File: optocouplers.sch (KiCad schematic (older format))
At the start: 20 parts, among them J901 Conn_01x04, Q901 MMBT5551L, U901 EL3H7(C)(TA)-G, U902 EL3H7(C)(TA)-G

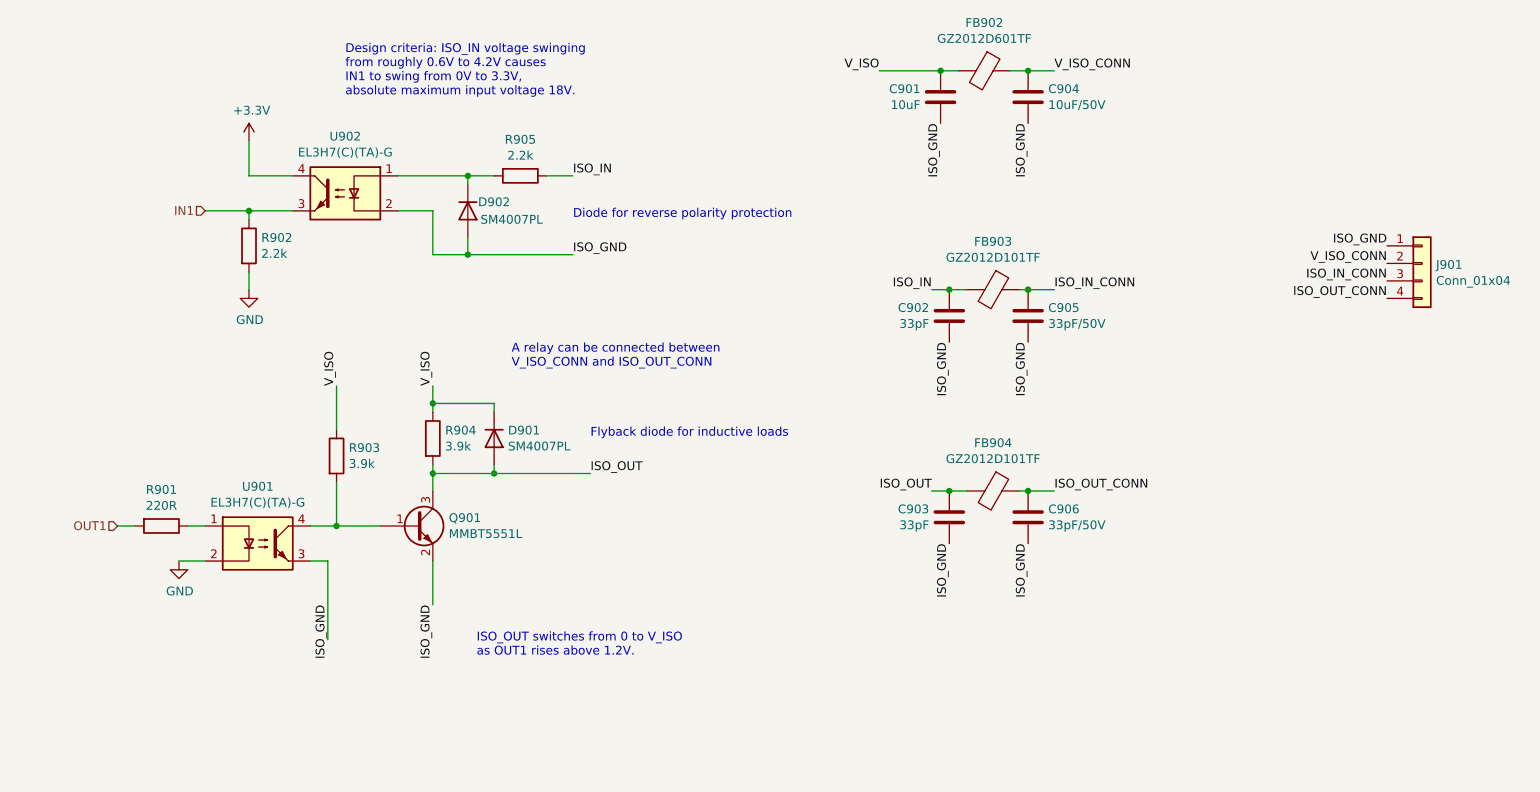
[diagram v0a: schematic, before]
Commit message: Add an unpopulated pad for extra opto output pullup
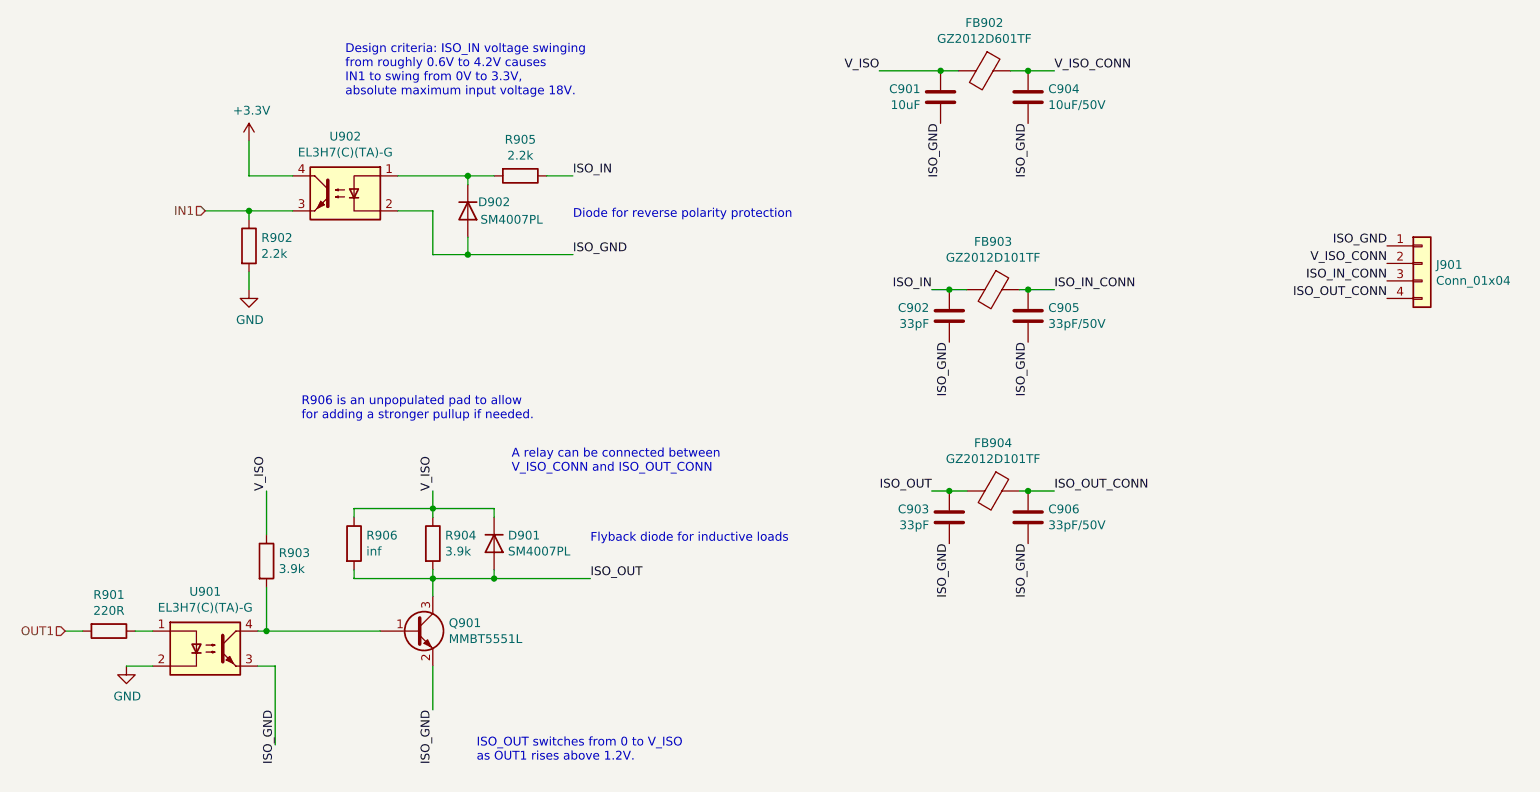
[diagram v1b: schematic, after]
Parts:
- added R906: inf, Resistor_SMD:R_0805_2012Metric, symbol Device:R
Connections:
- net ISO_OUT: now also R906.2
- net V_ISO: now also R906.1
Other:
- note added: "R906 is an unpopulated pad to allow\nfor adding a stronger pullup if needed."
- moved on the sheet: D901, Q901, R901, R903, R904, U901
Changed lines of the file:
@@
 $Descr A4 11693 8268
 encoding utf-8
-Sheet 10 11
+Sheet 9 11
 Title "Sailor Hat for ESP32"
 Date ""
@@
 L Device:R R901
 U 1 1 5FB305CD
-P 2350 4300
-F 0 "R901" V 2143 4300 50  0000 C CNN
-F 1 "220R" V 2234 4300 50  0000 C CNN
-F 2 "Resistor_SMD:R_0603_1608Metric" V 2280 4300 50  0001 C CNN
-F 3 "~" H 2350 4300 50  0001 C CNN
-F 4 "C22962" H 2350 4300 50  0001 C CNN "LCSC"
-	1    2350 4300
+P 2050 4900
+F 0 "R901" V 1843 4900 50  0000 C CNN
+F 1 "220R" V 1934 4900 50  0000 C CNN
+F 2 "Resistor_SMD:R_0603_1608Metric" V 1980 4900 50  0001 C CNN
+F 3 "~" H 2050 4900 50  0001 C CNN
+F 4 "C22962" H 2050 4900 50  0001 C CNN "LCSC"
+	1    2050 4900
 	0    1    1    0
 $EndComp
@@
 L power:GND #PWR0901
 U 1 1 5FB3123D
-P 2450 4500
-F 0 "#PWR0901" H 2450 4250 50  0001 C CNN
-F 1 "GND" H 2455 4327 50  0000 C CNN
-F 2 "" H 2450 4500 50  0001 C CNN
-F 3 "" H 2450 4500 50  0001 C CNN
-	1    2450 4500
-	1    0    0    -1
-$EndComp
-Wire Wire Line
-	2450 4500 2600 4500
-Wire Wire Line
-	2600 4300 2500 4300
-Wire Wire Line
-	2200 4300 2100 4300
+P 2150 5100
+F 0 "#PWR0901" H 2150 4850 50  0001 C CNN
+F 1 "GND" H 2155 4927 50  0000 C CNN
+F 2 "" H 2150 5100 50  0001 C CNN
+F 3 "" H 2150 5100 50  0001 C CNN
+	1    2150 5100
+	1    0    0    -1
+$EndComp
+Wire Wire Line
+	2150 5100 2300 5100
+Wire Wire Line
+	2300 4900 2200 4900
+Wire Wire Line
+	1900 4900 1800 4900
 $Comp
 L Transistor_BJT:MMBT5551L Q901
 U 1 1 5FB347F2
-P 3800 4300
-F 0 "Q901" H 3991 4346 50  0000 L CNN
-F 1 "MMBT5551L" H 3991 4255 50  0000 L CNN
-F 2 "Package_TO_SOT_SMD:SOT-23" H 4000 4225 50  0001 L CIN
-F 3 "www.onsemi.com/pub/Collateral/MMBT5550LT1-D.PDF" H 3800 4300 50  0001 L CNN
-F 4 "C41095" H 3800 4300 50  0001 C CNN "LCSC"
-	1    3800 4300
+P 3800 4900
+F 0 "Q901" H 3991 4946 50  0000 L CNN
+F 1 "MMBT5551L" H 3991 4855 50  0000 L CNN
+F 2 "Package_TO_SOT_SMD:SOT-23" H 4000 4825 50  0001 L CIN
+F 3 "www.onsemi.com/pub/Collateral/MMBT5550LT1-D.PDF" H 3800 4900 50  0001 L CNN
+F 4 "C41095" H 3800 4900 50  0001 C CNN "LCSC"
+	1    3800 4900
 	1    0    0    -1
 $EndComp
@@
 L Device:R R903
 U 1 1 5FB354D0
-P 3350 3900
-F 0 "R903" H 3420 3946 50  0000 L CNN
-F 1 "3.9k" H 3420 3855 50  0000 L CNN
-F 2 "Resistor_SMD:R_0603_1608Metric" V 3280 3900 50  0001 C CNN
-F 3 "~" H 3350 3900 50  0001 C CNN
-F 4 "C23018" H 3350 3900 50  0001 C CNN "LCSC"
-	1    3350 3900
+P 2950 4500
+F 0 "R903" H 3020 4546 50  0000 L CNN
+F 1 "3.9k" H 3020 4455 50  0000 L CNN
+F 2 "Resistor_SMD:R_0603_1608Metric" V 2880 4500 50  0001 C CNN
+F 3 "~" H 2950 4500 50  0001 C CNN
+F 4 "C23018" H 2950 4500 50  0001 C CNN "LCSC"
+	1    2950 4500
 	1    0    0    -1
 $EndComp
@@
 L Device:R R904
 U 1 1 5FB36FDC
-P 3900 3800
-F 0 "R904" H 3970 3846 50  0000 L CNN
-F 1 "3.9k" H 3970 3755 50  0000 L CNN
-F 2 "Resistor_SMD:R_0603_1608Metric" V 3830 3800 50  0001 C CNN
-F 3 "~" H 3900 3800 50  0001 C CNN
-F 4 "C23018" H 3900 3800 50  0001 C CNN "LCSC"
-	1    3900 3800
-	1    0    0    -1
-$EndComp
-Wire Wire Line
-	3350 3750 3350 3500
-Wire Wire Line
-	3900 3650 3900 3600
-Wire Wire Line
-	3200 4300 3350 4300
-Wire Wire Line
-	3350 4050 3350 4300
-Connection ~ 3350 4300
-Wire Wire Line
-	3350 4300 3600 4300
-Wire Wire Line
-	3900 3950 3900 4000
-Connection ~ 3900 4000
-Wire Wire Line
-	3900 4000 3900 4100
-Wire Wire Line
-	3900 4500 3900 4750
-Wire Wire Line
-	3300 4950 3300 4500
-Wire Wire Line
-	3300 4500 3200 4500
-Text Label 3900 4750 3    50   ~ 0
-ISO_GND
-Text Label 4800 4000 0    50   ~ 0
+P 3900 4400
+F 0 "R904" H 3970 4446 50  0000 L CNN
+F 1 "3.9k" H 3970 4355 50  0000 L CNN
+F 2 "Resistor_SMD:R_0603_1608Metric" V 3830 4400 50  0001 C CNN
+F 3 "~" H 3900 4400 50  0001 C CNN
+F 4 "C23018" H 3900 4400 50  0001 C CNN "LCSC"
+	1    3900 4400
+	1    0    0    -1
+$EndComp
+Wire Wire Line
+	2950 4350 2950 4100
+Wire Wire Line
+	3900 4250 3900 4200
+Wire Wire Line
+	2900 4900 2950 4900
+Wire Wire Line
+	2950 4650 2950 4900
+Wire Wire Line
+	3900 4550 3900 4600
+Connection ~ 3900 4600
+Wire Wire Line
+	3900 4600 3900 4700
+Wire Wire Line
+	3900 5100 3900 5350
+Wire Wire Line
+	3000 5550 3000 5100
+Wire Wire Line
+	3000 5100 2900 5100
+Text Label 3900 5350 3    50   ~ 0
+ISO_GND
+Text Label 4800 4600 0    50   ~ 0
 ISO_OUT
-Text Label 3350 3500 1    50   ~ 0
+Text Label 2950 4100 1    50   ~ 0
 V_ISO
-Text Label 3900 3500 1    50   ~ 0
+Text Label 3900 4100 1    50   ~ 0
 V_ISO
 Text Label 4700 2750 0    50   ~ 0
@@
 ISO_GND
 Wire Wire Line
-	3900 4000 4250 4000
+	3900 4600 4250 4600
 Text HLabel 2600 2500 0    50   Input ~ 0
 IN1
-Text HLabel 2100 4300 0    50   Input ~ 0
+Text HLabel 1800 4900 0    50   Input ~ 0
 OUT1
 $Comp
 L Device:D D?
 U 1 1 5FC24243
-P 4250 3800
+P 4250 4400
 AR Path="/5C3476D8/5FC24243" Ref="D?"  Part="1"
 AR Path="/5CA65CC5/5FC24243" Ref="D?"  Part="1"
 AR Path="/5F6FAF6E/5FC24243" Ref="D?"  Part="1"
 AR Path="/5FB2AE13/5FC24243" Ref="D901"  Part="1"
-F 0 "D901" V 4204 3879 50  0000 L CNN
-F 1 "SM4007PL" V 4295 3879 50  0000 L CNN
-F 2 "Diode_SMD:D_SOD-123F" H 4250 3800 50  0001 C CNN
-F 3 "~" H 4250 3800 50  0001 C CNN
-F 4 "" V 4250 3800 50  0001 C CNN "Notes"
-F 5 "C64898" H 4250 3800 50  0001 C CNN "LCSC"
-	1    4250 3800
-	0    1    1    0
-$EndComp
-Text Notes 4350 3400 0    50   ~ 0
+F 0 "D901" V 4204 4479 50  0000 L CNN
+F 1 "SM4007PL" V 4295 4479 50  0000 L CNN
+F 2 "Diode_SMD:D_SOD-123F" H 4250 4400 50  0001 C CNN
+F 3 "~" H 4250 4400 50  0001 C CNN
+F 4 "" V 4250 4400 50  0001 C CNN "Notes"
+F 5 "C64898" H 4250 4400 50  0001 C CNN "LCSC"
+	1    4250 4400
+	0    1    1    0
+$EndComp
+Text Notes 4350 4000 0    50   ~ 0
 A relay can be connected between\nV_ISO_CONN and ISO_OUT_CONN
 Wire Wire Line
-	4250 4000 4250 3950
-Connection ~ 4250 4000
-Wire Wire Line
-	4250 4000 4800 4000
-Wire Wire Line
-	4250 3650 4250 3600
-Wire Wire Line
-	4250 3600 3900 3600
-Connection ~ 3900 3600
-Wire Wire Line
-	3900 3600 3900 3500
+	4250 4600 4250 4550
+Connection ~ 4250 4600
+Wire Wire Line
+	4250 4600 4800 4600
+Wire Wire Line
+	4250 4250 4250 4200
+Wire Wire Line
+	4250 4200 3900 4200
+Connection ~ 3900 4200
+Wire Wire Line
+	3900 4200 3900 4100
 $Comp
 L Connector_Generic:Conn_01x04 J901
@@
 Text Notes 3400 1850 0    50   ~ 0
 Design criteria: ISO_IN voltage swinging \nfrom roughly 0.6V to 4.2V causes \nIN1 to swing from 0V to 3.3V,\nabsolute maximum input voltage 18V.
-Text Notes 4150 5050 0    50   ~ 0
+Text Notes 4150 5650 0    50   ~ 0
 ISO_OUT switches from 0 to V_ISO\nas OUT1 rises above 1.2V.
-Text Label 3300 4750 3    50   ~ 0
+Text Label 3000 5350 3    50   ~ 0
 ISO_GND
 Wire Wire Line
@@
 Text Notes 4700 2550 0    50   ~ 0
 Diode for reverse polarity protection
-Text Notes 4800 3800 0    50   ~ 0
+Text Notes 4800 4400 0    50   ~ 0
 Flyback diode for inductive loads
 $Comp
@@
 L SH-ESP32:EL3H7 U901
 U 1 1 5FCB38F6
-P 2900 4400
-F 0 "U901" H 2900 4725 50  0000 C CNN
-F 1 "EL3H7(C)(TA)-G" H 2900 4634 50  0000 C CNN
-F 2 "Package_SO:SOP-4_4.4x2.6mm_P1.27mm" H 2700 4200 50  0001 L CIN
-F 3 "http://www.sharpsme.com/download/pc3h4-epdf" H 2925 4400 50  0001 L CNN
-F 4 "C92243" H 2900 4400 50  0001 C CNN "LCSC"
-	1    2900 4400
-	1    0    0    -1
-$EndComp
+P 2600 5000
+F 0 "U901" H 2600 5325 50  0000 C CNN
+F 1 "EL3H7(C)(TA)-G" H 2600 5234 50  0000 C CNN
+F 2 "Package_SO:SOP-4_4.4x2.6mm_P1.27mm" H 2400 4800 50  0001 L CIN
+F 3 "http://www.sharpsme.com/download/pc3h4-epdf" H 2625 5000 50  0001 L CNN
+F 4 "C92243" H 2600 5000 50  0001 C CNN "LCSC"
+	1    2600 5000
+	1    0    0    -1
+$EndComp
+Connection ~ 2950 4900
+Wire Wire Line
+	2950 4900 3600 4900
+$Comp
+L Device:R R906
+U 1 1 5FC03D50
+P 3450 4400
+F 0 "R906" H 3520 4446 50  0000 L CNN
+F 1 "inf" H 3520 4355 50  0000 L CNN
+F 2 "Resistor_SMD:R_0805_2012Metric" V 3380 4400 50  0001 C CNN
+F 3 "~" H 3450 4400 50  0001 C CNN
+F 4 "" H 3450 4400 50  0001 C CNN "LCSC"
+	1    3450 4400
+	1    0    0    -1
+$EndComp
+Wire Wire Line
+	3450 4250 3450 4200
+Wire Wire Line
+	3450 4200 3900 4200
+Wire Wire Line
+	3450 4550 3450 4600
+Wire Wire Line
+	3450 4600 3900 4600
+Text Notes 3150 3700 0    50   ~ 0
+R906 is an unpopulated pad to allow\nfor adding a stronger pullup if needed.
 $EndSCHEMATC
